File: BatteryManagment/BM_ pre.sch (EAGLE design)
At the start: 19 parts, among them U1 ATMEGA328P-AU, U2 TPS54231DR

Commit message: Library update / Schematic 5V Buck Converter Delete
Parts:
- removed C10, C2, C4, C9: 47u, rcl:C-EUC0805
- removed C3: 10n, rcl:C-EUC0603
- removed C5: 15n, rcl:C-EUC0603
- removed C6: 1n, rcl:C-EUC0603
- removed C7: 47p, rcl:C-EUC0603
- removed C8: 100n, rcl:C-EUC0603
- removed L1_DR1050-100-R: 10u, inductors:DR1030
- removed R1: 330k, rcl:R-EU_R0603
- removed R2: 68k, rcl:R-EU_R0603
- removed R3: 29.4k, rcl:R-EU_R0603
- removed R4: 10.2k, rcl:R-EU_R0603
- removed R5: 3.24k, rcl:R-EU_R0603
- removed U$1: B240A, BM_pre:B240A
- removed U2: TPS54231DR, BM_pre:TPS54231DR
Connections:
- removed net N$14: C8.2, L1_DR1050-100-R.1, U$1.C, U2.PH
- removed net N$3: R1.1, R2.2, U2.EN
- removed net N$4: C5.1, U2.SS
- removed net N$5: C6.1, C7.1, U2.COMP
- removed net N$7: C6.2, R3.2
- removed net N$8: C8.1, U2.BOOT
- removed net V+: C2.1, C3.1, C4.1, R1.2, U2.VIN
- removed net VREF_3V3: R4.1, R5.2, U2.VSENSE
- net +3V3: no longer C10.1, C9.1, L1_DR1050-100-R.2, R4.2
- net GND: no longer C10.2, C2.2, C3.2, C4.2, C5.2, C7.2, C9.2, R2.1, R3.1, R5.1, U$1.A, U2.GND

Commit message: Worked at the Schematic
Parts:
- added BATTERY+: Battery+, BM_pre:PAD
- added BATTERY-: PAD, BM_pre:PAD
- added C10, C11, C9: 10u, rcl:C-EUC0805
- added C2, C7: 100n, rcl:C-EUC0603
- added C3, C6: 47u, rcl:C-EUC1812
- added C4, C5: 100u, rcl:CPOL-EUE3.5-10
- added C8: 1u_100V, rcl:C-EUC1206
- added CELL1, CELL2, CELL3, CELL4, CELL5, CELL6, GND, GND14, VIN: TPSQB2,54, testpad:TPSQB2,54
- added L1: 2310-V-RC, BM_pre:2310-V-RC
- added R1: 100k, rcl:R-EU_R0603
- added R10, R11, R12, R13, R2, R3, R4, R5, R6, R7, R8, R9: (no value), rcl:R-EU_R0603
- added U$1, U$3, U$5: SBR10B45P5, BM_pre:SBR10B45P5
- added U$2: IRFS7534-7PPBF, BM_pre:IRFS7534-7PPBF
- added U$4: CRA2512-FZ-R010ELF, BM_pre:CRA2512-FZ-R010ELF
- added U$6: IPB180P04P4L-02, BM_pre:IPB180P04P4L-02
- added U$7: ZXTR2012Z, BM_pre:ZXTR2012Z
- added U$8: NCV78L00A, BM_pre:NCV78L00A
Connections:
- removed net +3V3: C1.1, U1.AVCC, U1.VCC, U1.VCC_2
- new net +12V: C10.1, U$7.VO
- new net +5V: C1.1, C11.1, U$8.VO, U1.AREF, U1.AVCC, U1.VCC, U1.VCC_2
- new net ADC_BAT_1: R2.1, R3.2, U1.PC0
- new net ADC_BAT_2: R4.1, R5.2, U1.PC1
- new net ADC_BAT_3: R6.1, R7.2, U1.PC2
- new net ADC_BAT_4: R11.2, R8.1, U1.PC3
- new net ADC_BAT_5: R12.2, R9.1, U1.PC4
- new net ADC_BAT_6: R10.1, R13.2, U1.PC5
- new net BATTERY+: C9.1, R1.1, U$5.C, U$6.S, U$8.VI
- new net CURRENT+: L1.2, U$4.1
- new net CURRENT-: C5.+, C6.1, C7.1, U$4.2, U$5.A
- new net CURRENTSENSE: U1.ADC6
- new net LOAD_CONTROL: U$2.G
- new net MOTOR+: BATTERY+.TP, U$6.D
- new net MOTOR_CONTROL: R1.2, U$6.G
- new net N$1: C2.1, C3.1, C4.+, U$1.C, U$2.S
- new net N$11: CELL3.TP, R6.2
- new net N$12: CELL4.TP, R8.2
- new net N$13: CELL5.TP, R9.2
- new net N$14: CELL6.TP, R10.2
- new net N$2: L1.1, U$2.D, U$3.C
- new net N$7: CELL1.TP, R2.2
- new net N$8: CELL2.TP, R4.2
- new net VIN_SENSE: C8.1, U$1.A, U$7.VI, U1.ADC7, VIN.TP
- net GND: now also BATTERY-.TP, C10.2, C11.2, C2.2, C3.2, C4.-, C5.-, C6.2, C7.2, C8.2, C9.2, GND.TP, GND14.TP, R11.1, R12.1, R13.1, R3.1, R5.1, R7.1, U$3.A, U$7.GND, U$8.GND
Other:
- note added: "NPN-Transistor"

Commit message: Upload it, that i can work at the PC
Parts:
- added R14, R15, R16, R17, R18, R19: (no value), rcl:R-EU_R0603
- added U$10, U$11, U$12, U$13, U$14, U$15, U$16, U$17, U$18, U$19, U$20, U$9: BC817, BM_pre:BC817
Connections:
- new net C1_B: U$15.B
- new net C2_B: U$16.B
- new net C3_B: U$17.B
- new net C4_B: U$18.B
- new net C5_B: U$19.B
- new net C6_B: U$20.B
- new net CELL1: CELL1.TP, R15.1, U$15.C, U$9.C
- new net CELL2: CELL2.TP, R16.1, U$10.C, U$16.C
- new net CELL3: CELL3.TP, R17.1, U$11.C, U$17.C
- new net CELL4: CELL4.TP, R18.1, U$12.C, U$18.C
- new net CELL5: CELL5.TP, R19.1, U$13.C, U$19.C
- new net CELL6: CELL6.TP, U$14.C, U$20.C
- new net N$10: R10.2, U$14.E
- new net N$3: R2.2, U$9.E
- new net N$4: R4.2, U$10.E
- new net N$5: R14.2, U$15.E
- new net N$6: R15.2, U$16.E
- new net N$9: R9.2, U$13.E
- new net V_MEAS: U$10.B, U$11.B, U$12.B, U$13.B, U$14.B, U$9.B
- net GND: now also R14.1
- net N$11: now also R16.2, U$17.E; no longer CELL3.TP, R6.2
- net N$12: now also R17.2, U$18.E; no longer CELL4.TP, R8.2
- net N$13: now also R18.2, U$19.E; no longer CELL5.TP, R9.2
- net N$14: now also R19.2, U$20.E; no longer CELL6.TP, R10.2
- net N$7: now also R6.2, U$11.E; no longer CELL1.TP, R2.2
- net N$8: now also R8.2, U$12.E; no longer CELL2.TP, R4.2
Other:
- note removed: "NPN-Transistor"
- moved on the sheet: CELL1, CELL2, CELL3, CELL4, CELL5, CELL6, GND14, R10, R11, R12, R13, R2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

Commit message: schematic ready to layout
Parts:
- added C12: 100n, rcl:C-EUC0603
- added D1: 1N4004, diode:1N4004
- added IC1: LMV321M5, BM_pre:LMV321M5
- added R20: 10k, rcl:R-EU_R0603
- added R21, R22: 1k, rcl:R-EU_R0603
- added R23, R24: 66k, rcl:R-EU_R0603
- added SV1: (no value), con-lstb:MA03-2
- added U$21: BC817, BM_pre:BC817
- added U2: LTC4440EMS8E-5PBF, BM_pre:LTC4440EMS8E-5PBF
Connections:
- removed net LOAD_CONTROL: U$2.G
- new net CHARGE_CONTROL: C12.2, D1.C, U$2.G, U2.TG
- new net CHARGE_PWM: U1.PB6, U2.INP
- new net MISO: SV1.6, U1.PB4
- new net MOSI: SV1.3, U1.PB3
- new net N$15: IC1.+IN, R21.1, R23.2
- new net N$16: IC1.-IN, R22.1, R24.2
- new net RESETICSP: R20.1, SV1.2, U1.PC6
- new net SCK: SV1.4, U1.PB5
- new net TS: L1.1, U$2.D, U$3.C, U2.TS
- new net UC_M_CONT: U$21.B, U1.PD7
- net +12V: now also D1.A, U2.VCC
- net +5V: now also IC1.V+, R20.2, SV1.5
- net C1_B: now also U1.PD0
- net C2_B: now also U1.PD1
- net C3_B: now also U1.PD2
- net C4_B: now also U1.PD3
- net C5_B: now also U1.PD4
- net C6_B: now also U1.PD5
- net CURRENT+: now also R21.2
- net CURRENT-: now also R22.2
- net CURRENTSENSE: now also IC1.OUT, R23.1, R24.1
- net GND: now also IC1.V-, SV1.1, U$21.C, U2.GND, U2.GND_2
- net MOTOR_CONTROL: now also U$21.E
- net N$2: now also C12.1, U2.BOOST; no longer L1.1, U$2.D, U$3.C
- net V_MEAS: now also U1.PD6

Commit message: just updating my pc
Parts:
- removed R2: (no value), rcl:R-EU_R0603
- added LED1, LED2, LED3: (no value), eagle-ltspice:LED_E
- added PAD1, PAD2: (no value), wirepad:SMD5
- added R25, R26, R27: 330, rcl:R-EU_R0603
- added R28: (no value), rcl:R-EU_R0603
- added R29, R30: 1M, rcl:R-EU_R0603
- added U$22, U$23: IPB180P04P4L-02, BM_pre:IPB180P04P4L-02
- added U$24: FDN306P, BM_pre:FDN306P
- added U$25: FDN337N, BM_pre:FDN337N
- C1: value (none) -> 100n
- GND, VIN: value TPSQB2,54 -> Battery+; device testpad:TPSQB2,54 -> BM_pre:PAD
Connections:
- removed net N$3: R2.2, U$9.E
- new net N$17: LED2.C, U1.PB0
- new net N$18: LED1.C, U1.PB1
- new net N$19: LED3.C, U1.PB2
- new net N$20: PAD1.P, R29.1, U$24.G, U$25.D
- new net N$21: R29.2, U$24.S
- new net N$23: LED2.A, R27.1
- new net N$24: LED1.A, R26.1
- new net N$25: LED3.A, R25.1
- new net N$26: R28.1, U$21.C
- new net SELBSTERHALTUNG: R30.2, U$25.G, U1.PB7
- net +5V: now also R25.2, R26.2, R27.2
- net ADC_BAT_1: now also U$9.E; no longer R2.1
- net BATTERY+: now also U$22.S, U$23.S, U$24.D
- net GND: now also PAD2.P, R28.2, R30.1, U$25.S, U2.NC; no longer U$21.C
- net MOTOR+: now also U$22.D, U$23.D
- net MOTOR_CONTROL: now also U$22.G, U$23.G
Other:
- note added: "Taster"
- moved on the sheet: C1, C10, C11, C8, C9, R20, SV1, U$7, U$8, U1

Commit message: layout update
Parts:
- added MOTOR+: Battery+, BM_pre:PAD
- added MOTOR-: PAD, BM_pre:PAD
- added R2, R31, R32, R33, R34, R35: (no value), rcl:R-EU_R0603
- BATTERY-: value PAD -> Battery+
- CELL1, CELL2, CELL3, CELL4, CELL5, CELL6, GND14: value TPSQB2,54 -> (none); device testpad:TPSQB2,54 -> wirepad:SMD5
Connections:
- net BATTERY+: now also BATTERY+.TP
- net CELL1: now also CELL1.P, R31.1; no longer CELL1.TP
- net CELL2: now also CELL2.P, R32.1; no longer CELL2.TP
- net CELL3: now also CELL3.P, R33.1; no longer CELL3.TP
- net CELL4: now also CELL4.P, R34.1; no longer CELL4.TP
- net CELL5: now also CELL5.P, R35.1; no longer CELL5.TP
- net CELL6: now also CELL6.P; no longer CELL6.TP
- net GND: now also GND14.P, MOTOR-.TP, R2.1; no longer GND14.TP
- net MOTOR+: now also MOTOR+.TP; no longer BATTERY+.TP
- net N$11: now also R32.2
- net N$12: now also R33.2
- net N$13: now also R34.2
- net N$14: now also R35.2
- net N$5: now also R2.2
- net N$6: now also R31.2
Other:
- moved on the sheet: BATTERY+, BATTERY-

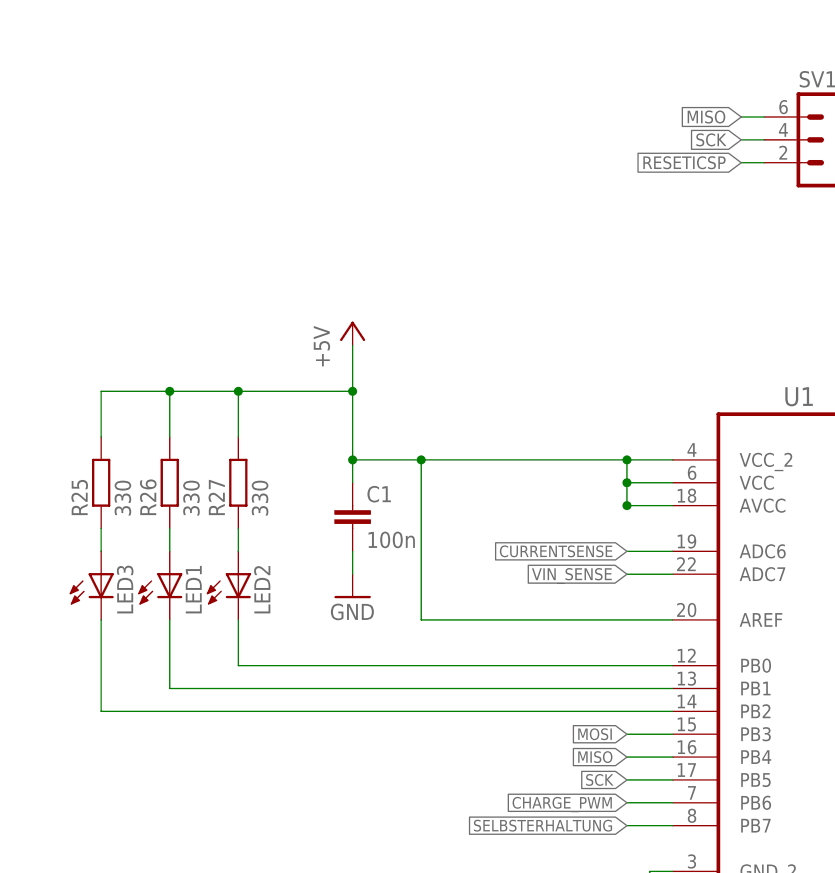
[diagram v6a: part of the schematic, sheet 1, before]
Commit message: Just GND Layout missing
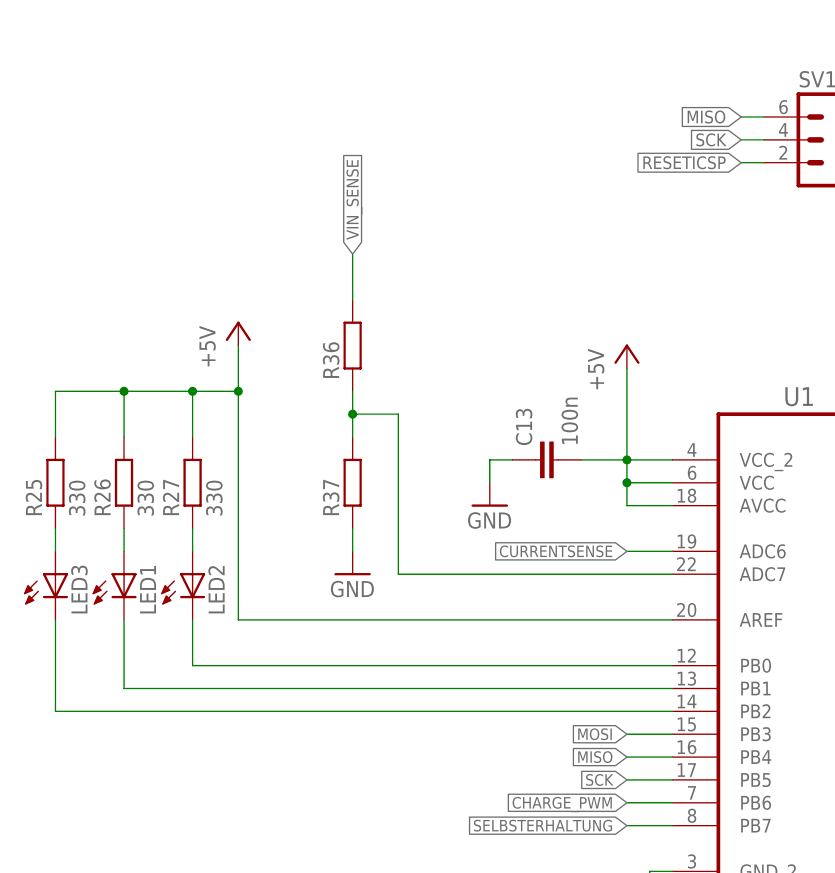
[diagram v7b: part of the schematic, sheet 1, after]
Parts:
- removed C1: 100n, eagle-ltspice:CC0603
- added C13: 100n, eagle-ltspice:CC0603
- added R36, R37: (no value), rcl:R-EU_R0603
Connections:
- removed net N$21: R29.2, U$24.S
- new net N$27: R36.1, R37.2, U1.ADC7
- new net TEST: C9.1, U$24.D, U$8.VI
- net +5V: now also C13.2; no longer C1.1
- net BATTERY+: now also R29.2, U$24.S; no longer C9.1, U$24.D, U$8.VI
- net GND: now also C13.1, R37.1; no longer C1.2
- net VIN_SENSE: now also R36.2; no longer U1.ADC7
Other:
- moved on the sheet: LED1, LED2, LED3, R25, R26, R27
